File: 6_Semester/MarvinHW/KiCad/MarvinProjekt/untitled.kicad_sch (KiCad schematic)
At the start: 3 parts, among them SW3 SW_DPST_x2, SW4 SW_DPST_x2

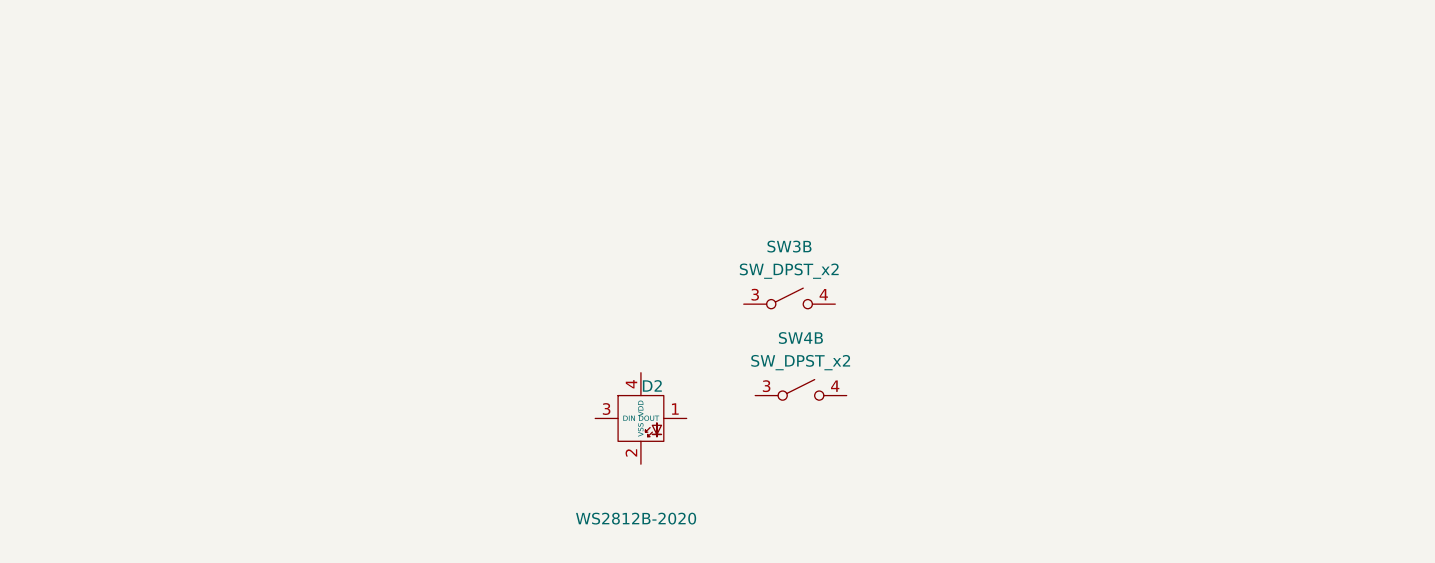
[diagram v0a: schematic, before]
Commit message: added datasheets and worked on schematic
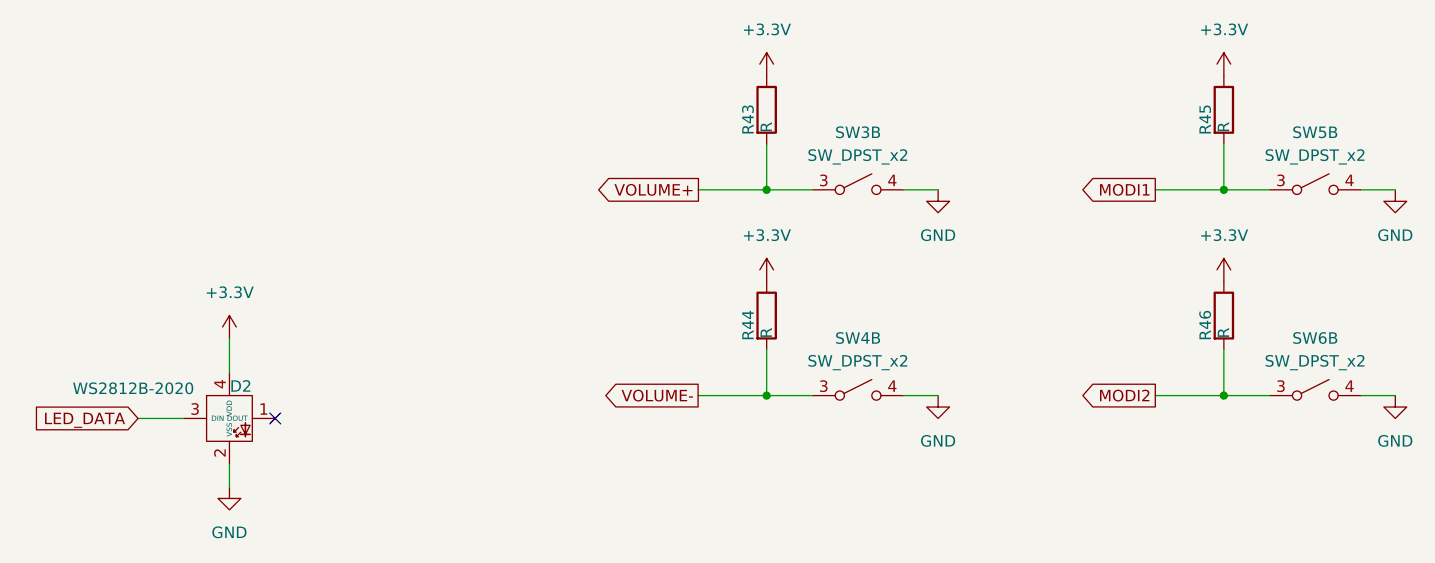
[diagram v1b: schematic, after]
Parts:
- added R43, R44, R45, R46: R, symbol Device:R
- added SW5, SW6: SW_DPST_x2, Matrix2_Schnuppiprojekt:Taster, symbol Switch:SW_DPST_x2
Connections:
- net GND: now reaches D2.2 (VSS)
- net GND: now also SW3.4 (B), SW4.4 (B), SW5.4 (B), SW6.4 (B)
- net LED_DATA: now reaches D2.3 (DIN)
- net +3.3V: now reaches D2.4 (VDD)
- net +3.3V: now also R43.1, R44.1, R45.1, R46.1
- net VOLUME-: now reaches SW4.3 (A)
- net VOLUME-: now also R44.2
- net VOLUME+: now reaches SW3.3 (A)
- net VOLUME+: now also R43.2
- new net MODI1: R45.2, SW5.3 (A)
- new net MODI2: R46.2, SW6.3 (A)
- no-connect marks 0 -> 1
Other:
- moved on the sheet: D2, SW3B, SW4B
